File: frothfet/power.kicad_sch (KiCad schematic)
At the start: 43 parts, among them J11 Screw_Terminal_01x08, J12 Screw_Terminal_01x08, U26 TPS7A2033PDBVR, U27 XL1509-5.0, U28 MCP3425A0T-ECH, U29 MAX40200AUK

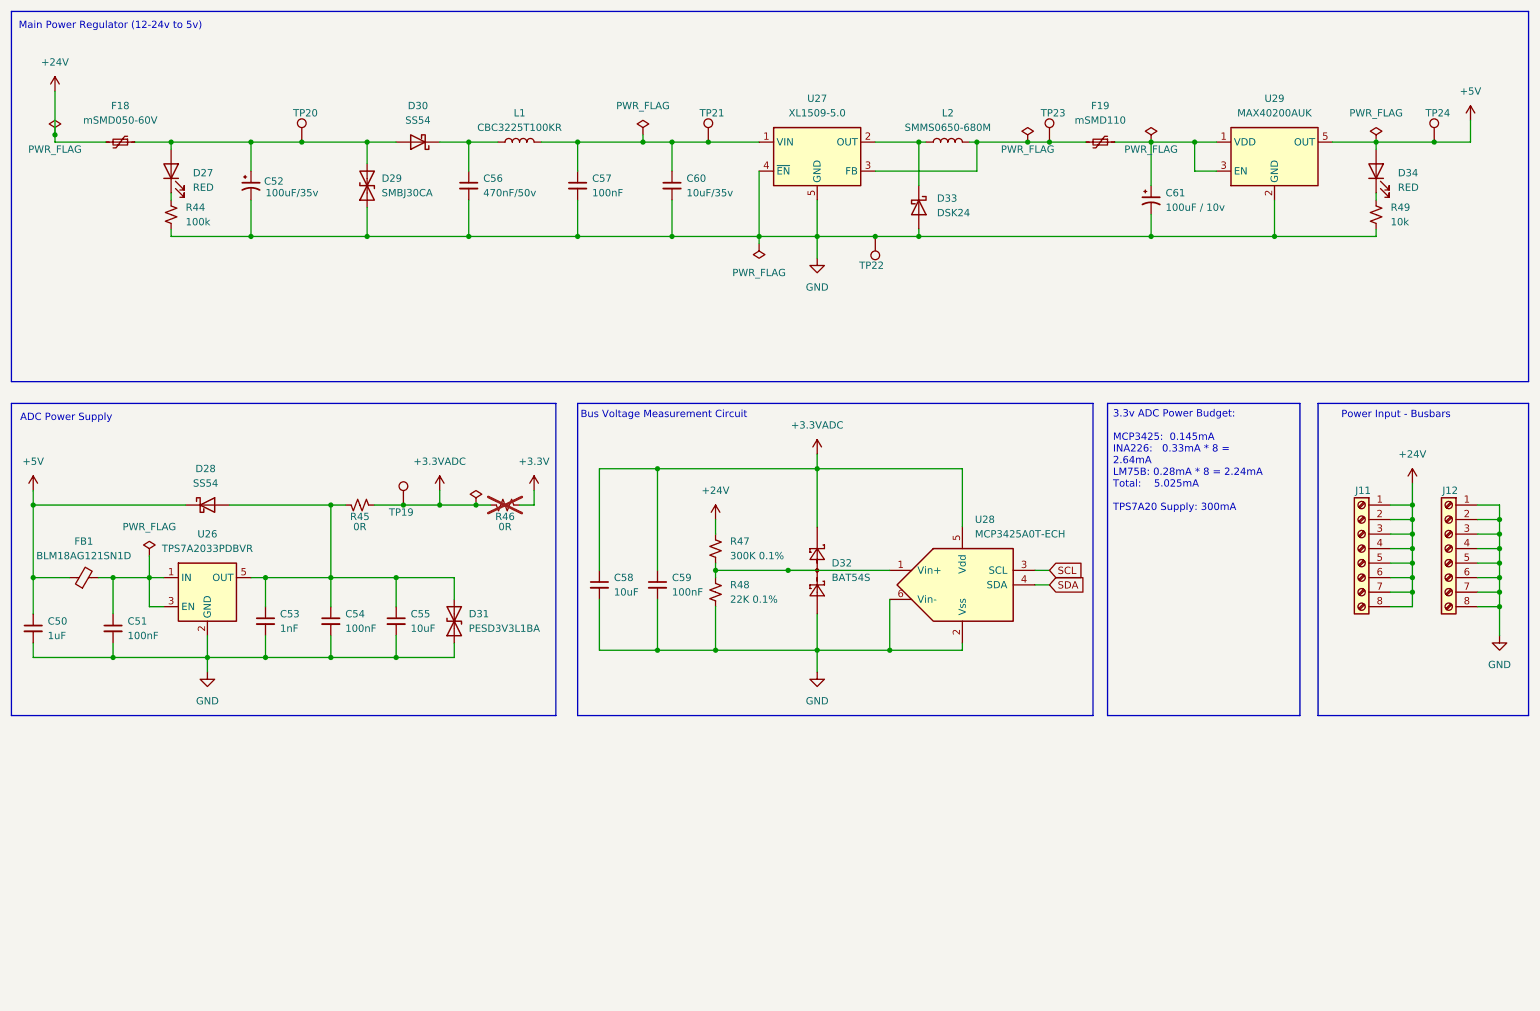
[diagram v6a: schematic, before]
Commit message: added more esd protection to 3.3v and 5v rails.
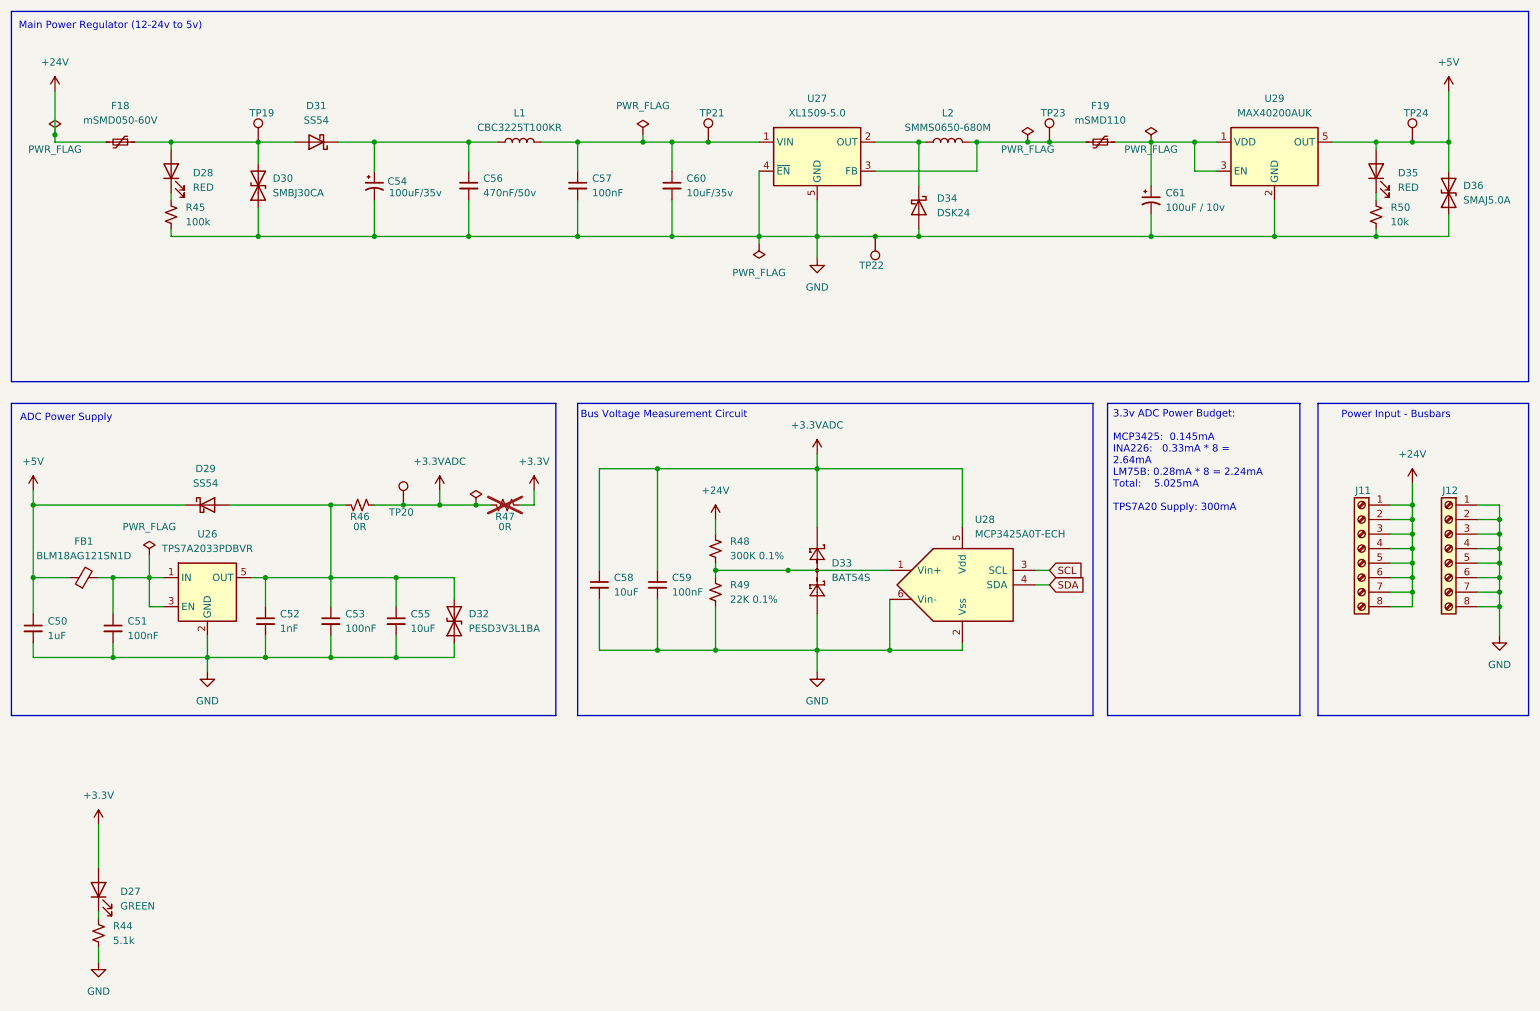
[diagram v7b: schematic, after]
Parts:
- added D27: GREEN, LED_SMD:LED_0603_1608Metric, symbol Device:LED
- added D36: SMAJ5.0A, Diode_SMD:D_SMA, symbol Device:D_TVS
- added R44: 5.1k, Resistor_SMD:R_0603_1608Metric, symbol Device:R_Small_US
- renumbered C53 to C52, C54 to C53, C52 to C54, D27 to D28, D28 to D29, D29 to D30, D30 to D31, D31 to D32, D32 to D33, D33 to D34, D34 to D35, R44 to R45, R45 to R46, R46 to R47, R47 to R48, R48 to R49, R49 to R50, TP20 to TP19, TP19 to TP20
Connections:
- net +3.3V: now also D27.2 (A)
- net +5V: now also D36.2 (A2)
- net GND: now also D36.1 (A1), R44.2
- net at D28.2 (A), D30.2 (A2), D31.2 (A)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: no longer C54.1
- net at C56.1, D31.1 (K), L1.1: now also C54.1
- new net: D27.1 (K), R44.1
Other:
- moved on the sheet: C54, D30, D31, TP19, TP24

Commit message: added support for ALERT pin from INA226 for overcurrent protection (hopefully)
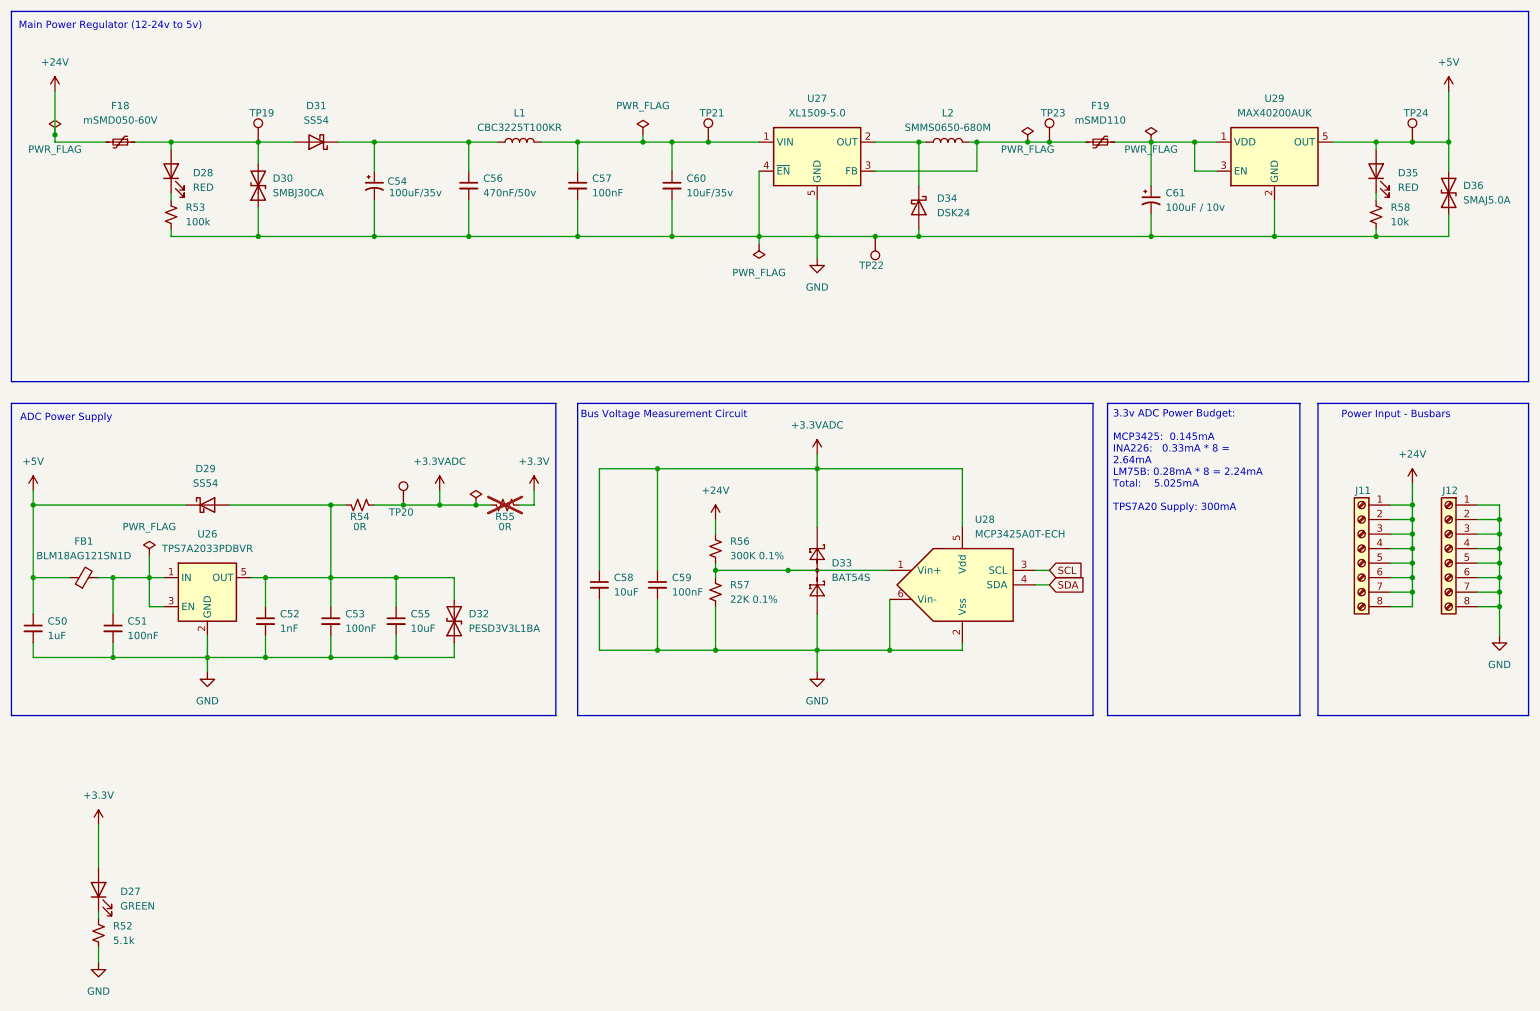
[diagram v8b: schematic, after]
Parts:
- renumbered R44 to R52, R45 to R53, R46 to R54, R47 to R55, R48 to R56, R49 to R57, R50 to R58
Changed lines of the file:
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@@
 		(dnp no)
 		(fields_autoplaced yes)
-		(property "Reference" "R45"
+		(property "Reference" "R53"
 			(at 45.72 49.5299 0)
 			(effects
@@
 			(project "frothfet"
 				(path "/c83c6236-96e9-46ad-9d7a-9e2efa4a7966/e112a34f-fd2f-43cb-bf5d-a7f5e57b6bef"
-					(reference "R45")
+					(reference "R53")
 					(unit 1)
 				)
@@
 		(dnp no)
 		(fields_autoplaced yes)
-		(property "Reference" "R50"
+		(property "Reference" "R58"
 			(at 256.54 49.5299 0)
 			(effects
@@
 			(project "frothfet"
 				(path "/c83c6236-96e9-46ad-9d7a-9e2efa4a7966/e112a34f-fd2f-43cb-bf5d-a7f5e57b6bef"
-					(reference "R50")
+					(reference "R58")
 					(unit 1)
 				)
@@
 		(dnp no)
 		(fields_autoplaced yes)
-		(property "Reference" "R48"
+		(property "Reference" "R56"
 			(at 140.97 107.95 0)
 			(effects
@@
 			(project "8ch-mosfet"
 				(path "/c83c6236-96e9-46ad-9d7a-9e2efa4a7966/e112a34f-fd2f-43cb-bf5d-a7f5e57b6bef"
-					(reference "R48")
+					(reference "R56")
 					(unit 1)
 				)
@@
 		(on_board yes)
 		(dnp no)
-		(property "Reference" "R46"
+		(property "Reference" "R54"
 			(at 76.2 103.632 90)
 			(effects
@@
 			(project "frothfet"
 				(path "/c83c6236-96e9-46ad-9d7a-9e2efa4a7966/e112a34f-fd2f-43cb-bf5d-a7f5e57b6bef"
-					(reference "R46")
+					(reference "R54")
 					(unit 1)
 				)
@@
 		(on_board yes)
 		(dnp yes)
-		(property "Reference" "R47"
+		(property "Reference" "R55"
 			(at 101.6 103.632 90)
 			(effects
@@
 			(project "frothfet"
 				(path "/c83c6236-96e9-46ad-9d7a-9e2efa4a7966/e112a34f-fd2f-43cb-bf5d-a7f5e57b6bef"
-					(reference "R47")
+					(reference "R55")
 					(unit 1)
 				)
@@
 		(dnp no)
 		(fields_autoplaced yes)
-		(property "Reference" "R49"
+		(property "Reference" "R57"
 			(at 140.97 115.57 0)
 			(effects
@@
 			(project "8ch-mosfet"
 				(path "/c83c6236-96e9-46ad-9d7a-9e2efa4a7966/e112a34f-fd2f-43cb-bf5d-a7f5e57b6bef"
-					(reference "R49")
+					(reference "R57")
 					(unit 1)
 				)
@@
 		(dnp no)
 		(fields_autoplaced yes)
-		(property "Reference" "R44"
+		(property "Reference" "R52"
 			(at 33.02 175.2599 0)
 			(effects
@@
 			(project "frothfet"
 				(path "/c83c6236-96e9-46ad-9d7a-9e2efa4a7966/e112a34f-fd2f-43cb-bf5d-a7f5e57b6bef"
-					(reference "R44")
+					(reference "R52")
 					(unit 1)
 				)
